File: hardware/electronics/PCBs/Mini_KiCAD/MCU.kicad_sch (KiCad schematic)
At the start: 21 parts, among them U1 RP2040, U2 W25Q16JVSS

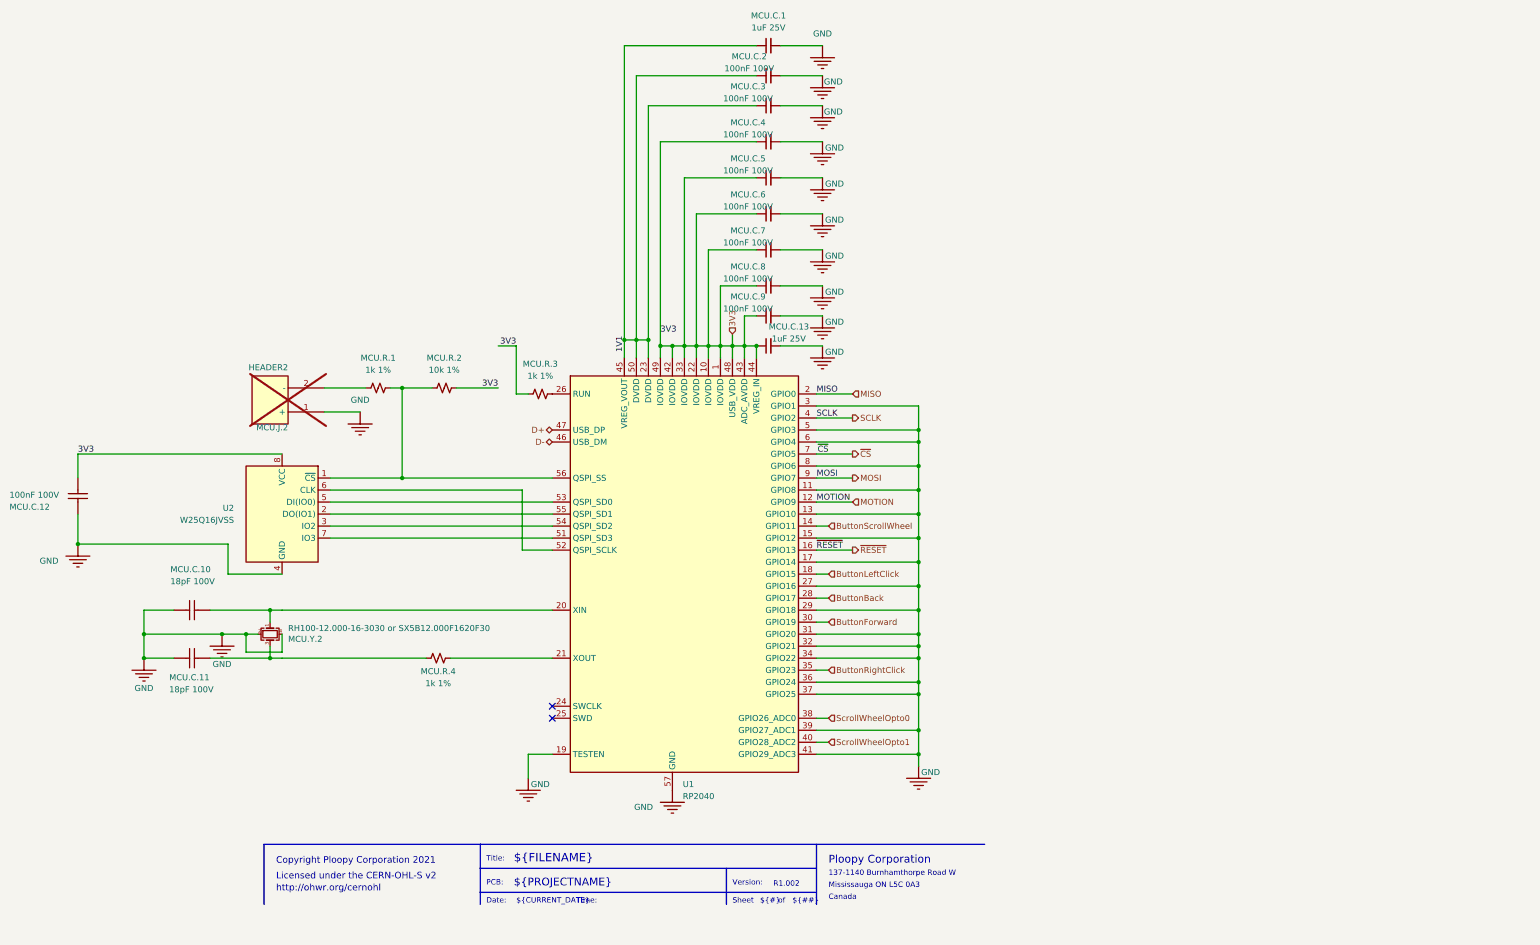
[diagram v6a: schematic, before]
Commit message: Rev1.002 Replaced all symbols in the schematic with built-in symbols where applicable. Reoriented the sensor to solve interference and tracking issues. Replaced the mid-mount USB port with regular port.
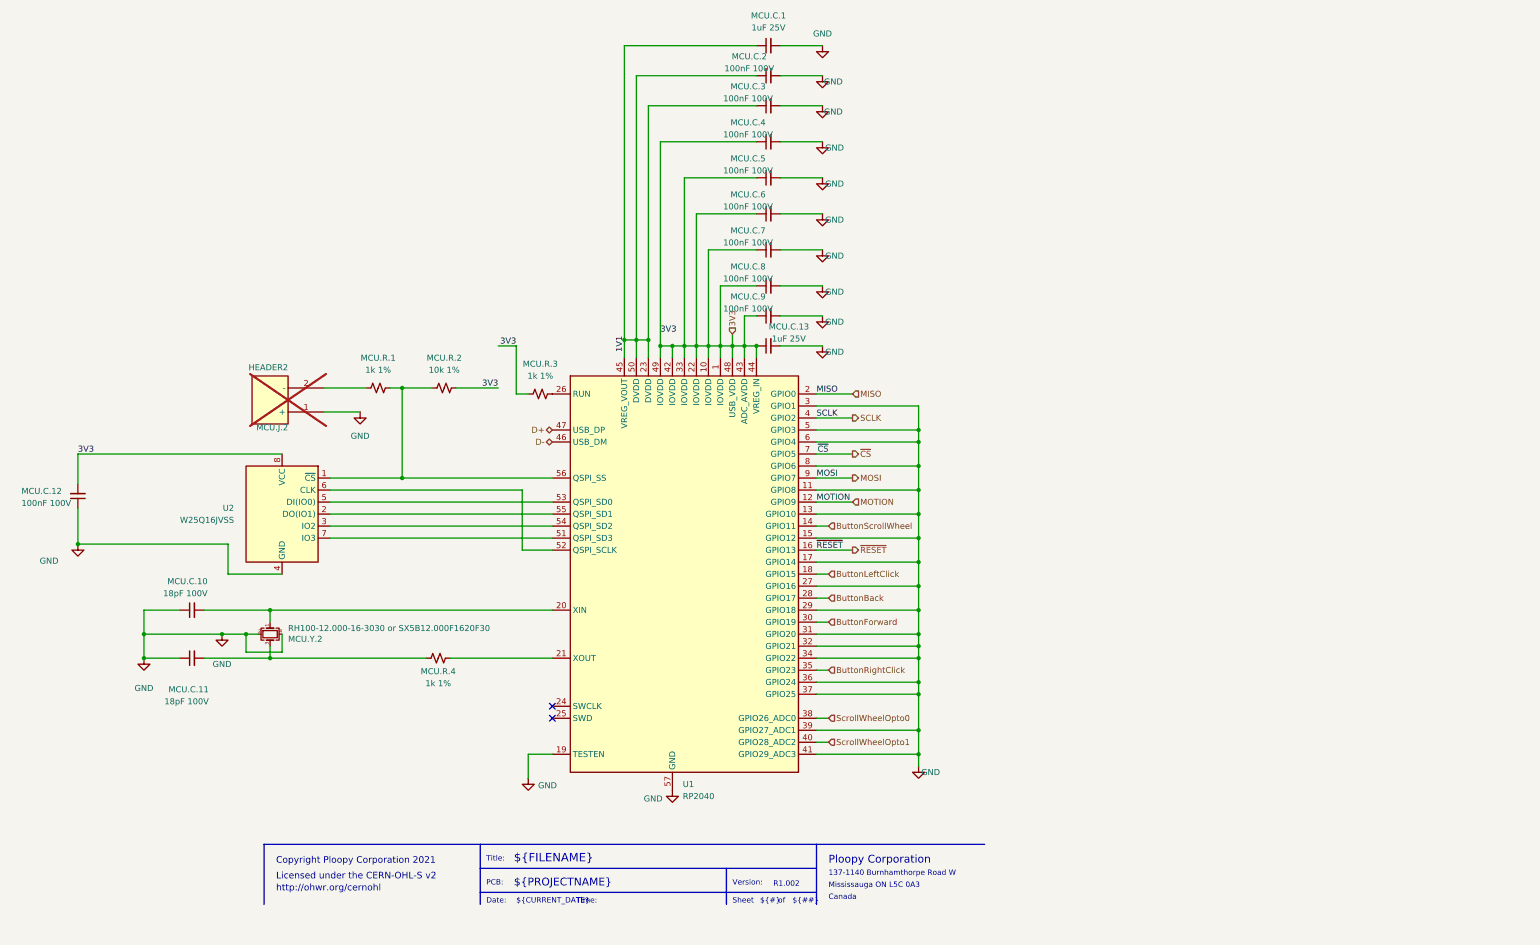
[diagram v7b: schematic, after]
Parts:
- MCU.C.10, MCU.C.11, MCU.C.12: symbol Mini-altium-import:MCU_1_Cap 0.1uF 100V -> Device:C_Small
